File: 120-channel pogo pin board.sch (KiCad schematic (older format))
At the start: 241 parts, among them P1 CONN_1, P10 CONN_1, P100 CONN_1, P101 CONN_1, P102 CONN_1, P103 CONN_1, P104 CONN_1, P105 CONN_1, P106 CONN_1, P107 CONN_1, P108 CONN_1, P109 CONN_1, P11 CONN_1, P110 CONN_1, P111 CONN_1, P112 CONN_1, P113 CONN_1, P114 CONN_1, P115 CONN_1, P116 CONN_1, P117 CONN_1, P118 CONN_1, P119 CONN_1, P12 CONN_1, P120 CONN_1, P121 CONN_1, P13 CONN_1, P14 CONN_1, P15 CONN_1, P16 CONN_1, P17 CONN_1, P18 CONN_1, P19 CONN_1, P2 CONN_1, P20 CONN_1, P21 CONN_1, P22 CONN_1, P23 CONN_1, P24 CONN_1, P25 CONN_1, P26 CONN_1, P27 CONN_1, P28 CONN_1, P29 CONN_1, P3 CONN_1, P30 CONN_1, P31 CONN_1, P32 CONN_1, P33 CONN_1, P34 CONN_1, P35 CONN_1, P36 CONN_1, P37 CONN_1, P38 CONN_1, P39 CONN_1, P4 CONN_1, P40 CONN_1, P41 CONN_1, P42 CONN_1, P43 CONN_1, P44 CONN_1, P45 CONN_1, P46 CONN_1, P47 CONN_1, P48 CONN_1, P49 CONN_1, P5 CONN_1, P50 CONN_1, P51 CONN_1, P52 CONN_1, P53 CONN_1, P54 CONN_1, P55 CONN_1, P56 CONN_1, P57 CONN_1, P58 CONN_1, P59 CONN_1, P6 CONN_1, P60 CONN_1, P61 CONN_1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

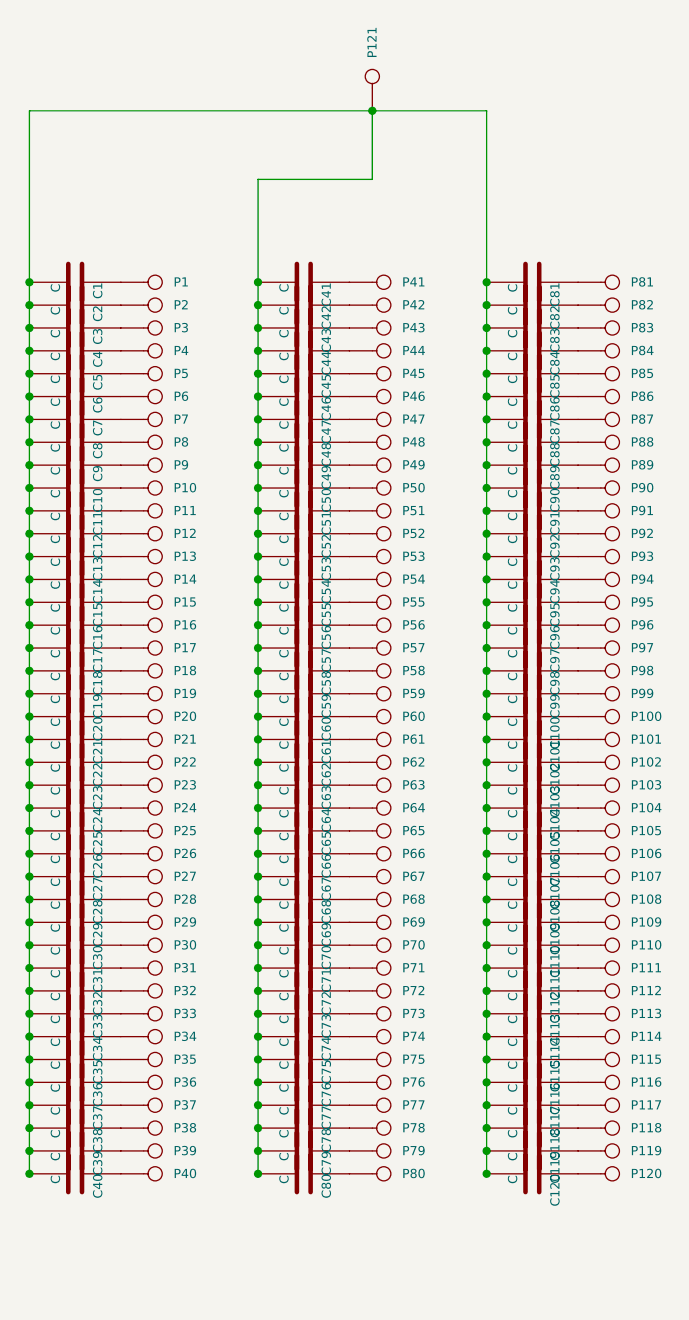
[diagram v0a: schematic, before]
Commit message: Upgrade to kicad v4.0.0 rc1
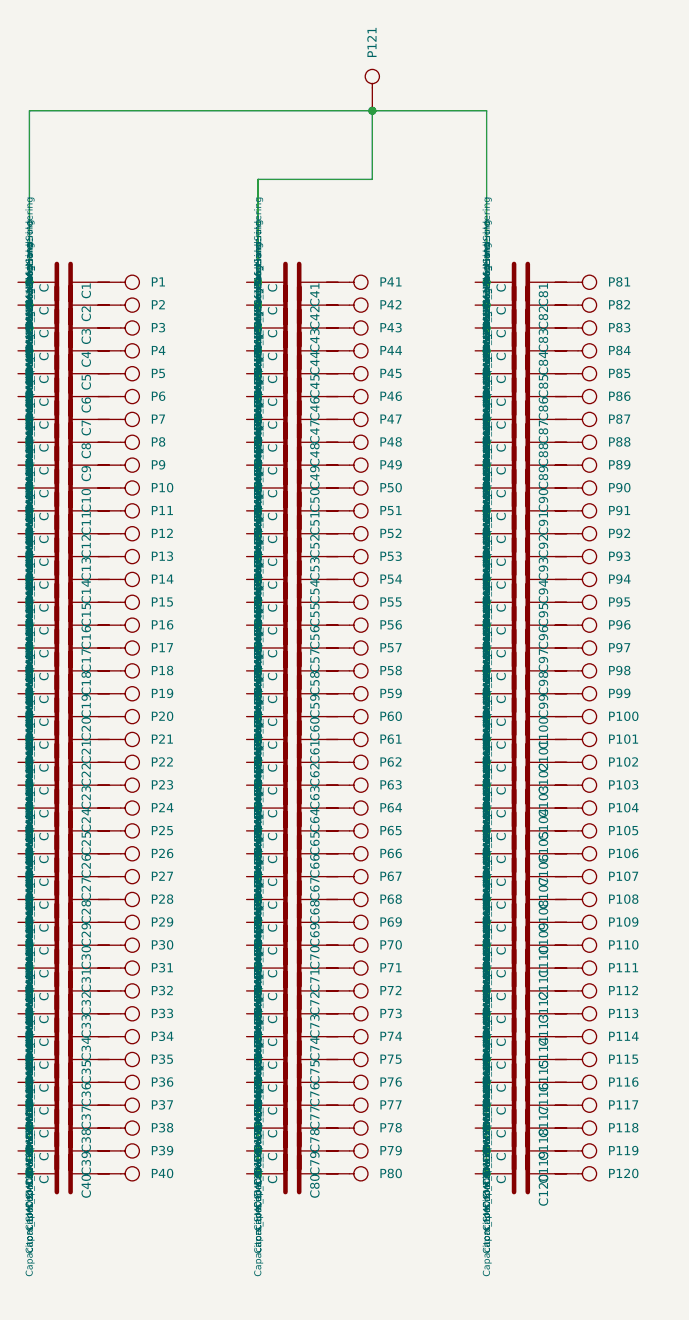
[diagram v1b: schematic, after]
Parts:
- C1, C10, C100, C101, C102, C103, C104, C105, C106, C107, C108, C109, C11, C110, C111, C112, C113, C114, C115, C116, C117, C118, C119, C12, C120, C13, C14, C15, C16, C17, C18, C19, C2, C20, C21, C22, C23, C24, C25, C26, C27, C28, C29, C3, C30, C31, C32, C33, C34, C35, C36, C37, C38, C39, C4, C40, C41, C42, C43, C44, C45, C46, C47, C48, C49, C5, C50, C51, C52, C53, C54, C55, C56, C57, C58, C59, C6, C60, C61, C62, C63, C64, C65, C66, C67, C68, C69, C7, C70, C71, C72, C73, C74, C75, C76, C77, C78, C79, C8, C80, C81, C82, C83, C84, C85, C86, C87, C88, C89, C9, C90, C91, C92, C93, C94, C95, C96, C97, C98, C99: footprint ~ -> Capacitors_SMD:C_1206_HandSoldering
- P1, P10, P100, P101, P102, P103, P104, P105, P106, P107, P108, P109, P11, P110, P111, P112, P113, P114, P115, P116, P117, P118, P119, P12, P120, P13, P14, P15, P16, P17, P18, P19, P2, P20, P21, P22, P23, P24, P25, P26, P27, P28, P29, P3, P30, P31, P32, P33, P34, P35, P36, P37, P38, P39, P4, P40, P41, P42, P43, P44, P45, P46, P47, P48, P49, P5, P50, P51, P52, P53, P54, P55, P56, P57, P58, P59, P6, P60, P61, P62, P63, P64, P65, P66, P67, P68, P69, P7, P70, P71, P72, P73, P74, P75, P76, P77, P78, P79, P8, P80, P81, P82, P83, P84, P85, P86, P87, P88, P89, P9, P90, P91, P92, P93, P94, P95, P96, P97, P98, P99: footprint (none) -> wheelerlab:1.4mm_DMF_Electrode
- P121: footprint (none) -> wheelerlab:3.9mm_DMF_Electrode
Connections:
- net at P1.1: no longer C1.1
- net at P2.1: no longer C2.1
- net at P4.1: no longer C4.1
- net at P3.1: no longer C3.1
- net at P5.1: no longer C5.1
- net at P10.1: no longer C10.1
- net at P8.1: no longer C8.1
- net at P9.1: no longer C9.1
- net at P7.1: no longer C7.1
- net at P6.1: no longer C6.1
- net at P15.1: no longer C15.1
- net at P13.1: no longer C13.1
- net at P14.1: no longer C14.1
- net at P12.1: no longer C12.1
- net at P11.1: no longer C11.1
- net at P20.1: no longer C20.1
- net at P18.1: no longer C18.1
- net at P19.1: no longer C19.1
- net at P17.1: no longer C17.1
- net at P16.1: no longer C16.1
- net at P25.1: no longer C25.1
- net at P23.1: no longer C23.1
- net at P24.1: no longer C24.1
- net at P22.1: no longer C22.1
- net at P21.1: no longer C21.1
- net at P30.1: no longer C30.1
- net at P28.1: no longer C28.1
- net at P29.1: no longer C29.1
- net at P27.1: no longer C27.1
- net at P26.1: no longer C26.1
- net at P35.1: no longer C35.1
- net at P33.1: no longer C33.1
- net at P34.1: no longer C34.1
- net at P32.1: no longer C32.1
- net at P31.1: no longer C31.1
- net at P40.1: no longer C40.1
- net at P38.1: no longer C38.1
- net at P39.1: no longer C39.1
- net at P37.1: no longer C37.1
- net at P36.1: no longer C36.1
- net at P45.1: no longer C45.1
- net at P43.1: no longer C43.1
- net at P44.1: no longer C44.1
- net at P42.1: no longer C42.1
- net at P41.1: no longer C41.1
- net at P50.1: no longer C50.1
- net at P48.1: no longer C48.1
- net at P49.1: no longer C49.1
- net at P47.1: no longer C47.1
- net at P46.1: no longer C46.1
- net at P55.1: no longer C55.1
- net at P53.1: no longer C53.1
- net at P54.1: no longer C54.1
- net at P52.1: no longer C52.1
- net at P51.1: no longer C51.1
- net at P60.1: no longer C60.1
- net at P58.1: no longer C58.1
- net at P59.1: no longer C59.1
- net at P57.1: no longer C57.1
- net at P56.1: no longer C56.1
- net at P65.1: no longer C65.1
- net at P63.1: no longer C63.1
- net at P64.1: no longer C64.1
- net at P62.1: no longer C62.1
- net at P61.1: no longer C61.1
- net at P70.1: no longer C70.1
- net at P68.1: no longer C68.1
- net at P69.1: no longer C69.1
- net at P67.1: no longer C67.1
- net at P66.1: no longer C66.1
- net at P75.1: no longer C75.1
- net at P73.1: no longer C73.1
- net at P74.1: no longer C74.1
- net at P72.1: no longer C72.1
- net at P71.1: no longer C71.1
- net at P80.1: no longer C80.1
- net at P78.1: no longer C78.1
- net at P79.1: no longer C79.1
- net at P77.1: no longer C77.1
- net at P76.1: no longer C76.1
- net at P85.1: no longer C85.1
- net at P83.1: no longer C83.1
- net at P84.1: no longer C84.1
- net at P82.1: no longer C82.1
- net at P81.1: no longer C81.1
- net at P90.1: no longer C90.1
- net at P88.1: no longer C88.1
- net at P89.1: no longer C89.1
- net at P87.1: no longer C87.1
- net at P86.1: no longer C86.1
- net at P95.1: no longer C95.1
- net at P93.1: no longer C93.1
- net at P94.1: no longer C94.1
- net at P92.1: no longer C92.1
- net at P91.1: no longer C91.1
- net at P100.1: no longer C100.1
- net at P98.1: no longer C98.1
- net at P99.1: no longer C99.1
- net at P97.1: no longer C97.1
- net at P96.1: no longer C96.1
- net at P105.1: no longer C105.1
- net at P103.1: no longer C103.1
- net at P104.1: no longer C104.1
- net at P102.1: no longer C102.1
- net at P101.1: no longer C101.1
- net at P110.1: no longer C110.1
- net at P108.1: no longer C108.1
- net at P109.1: no longer C109.1
- net at P107.1: no longer C107.1
- net at P106.1: no longer C106.1
- net at P115.1: no longer C115.1
- net at P113.1: no longer C113.1
- net at P114.1: no longer C114.1
- net at P112.1: no longer C112.1
- net at P111.1: no longer C111.1
- net at P120.1: no longer C120.1
- net at P118.1: no longer C118.1
- net at P119.1: no longer C119.1
- net at P117.1: no longer C117.1
- net at P116.1: no longer C116.1
- now unconnected: C1.2, C10.2, C100.2, C101.2, C102.2, C103.2, C104.2, C105.2, C106.2, C107.2, C108.2, C109.2, C11.2, C110.2, C111.2, C112.2, C113.2, C114.2, C115.2, C116.2, C117.2, C118.2, C119.2, C12.2, C120.2, C13.2, C14.2, C15.2, C16.2, C17.2, C18.2, C19.2, C2.2, C20.2, C21.2, C22.2, C23.2, C24.2, C25.2, C26.2, C27.2, C28.2, C29.2, C3.2, C30.2, C31.2, C32.2, C33.2, C34.2, C35.2, C36.2, C37.2, C38.2, C39.2, C4.2, C40.2, C41.2, C42.2, C43.2, C44.2, C45.2, C46.2, C47.2, C48.2, C49.2, C5.2, C50.2, C51.2, C52.2, C53.2, C54.2, C55.2, C56.2, C57.2, C58.2, C59.2, C6.2, C60.2, C61.2, C62.2, C63.2, C64.2, C65.2, C66.2, C67.2, C68.2, C69.2, C7.2, C70.2, C71.2, C72.2, C73.2, C74.2, C75.2, C76.2, C77.2, C78.2, C79.2, C8.2, C80.2, C81.2, C82.2, C83.2, C84.2, C85.2, C86.2, C87.2, C88.2, C89.2, C9.2, C90.2, C91.2, C92.2, C93.2, C94.2, C95.2, C96.2, C97.2, C98.2, C99.2, P121.1
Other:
- moved on the sheet: C1, C10, C100, C101, C102, C103, C104, C105, C106, C107, C108, C109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
